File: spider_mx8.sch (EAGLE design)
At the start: 4 parts, among them IC1 AVR-MEGA8-PPTH, J1 AVR_SPI_PRG_6NS

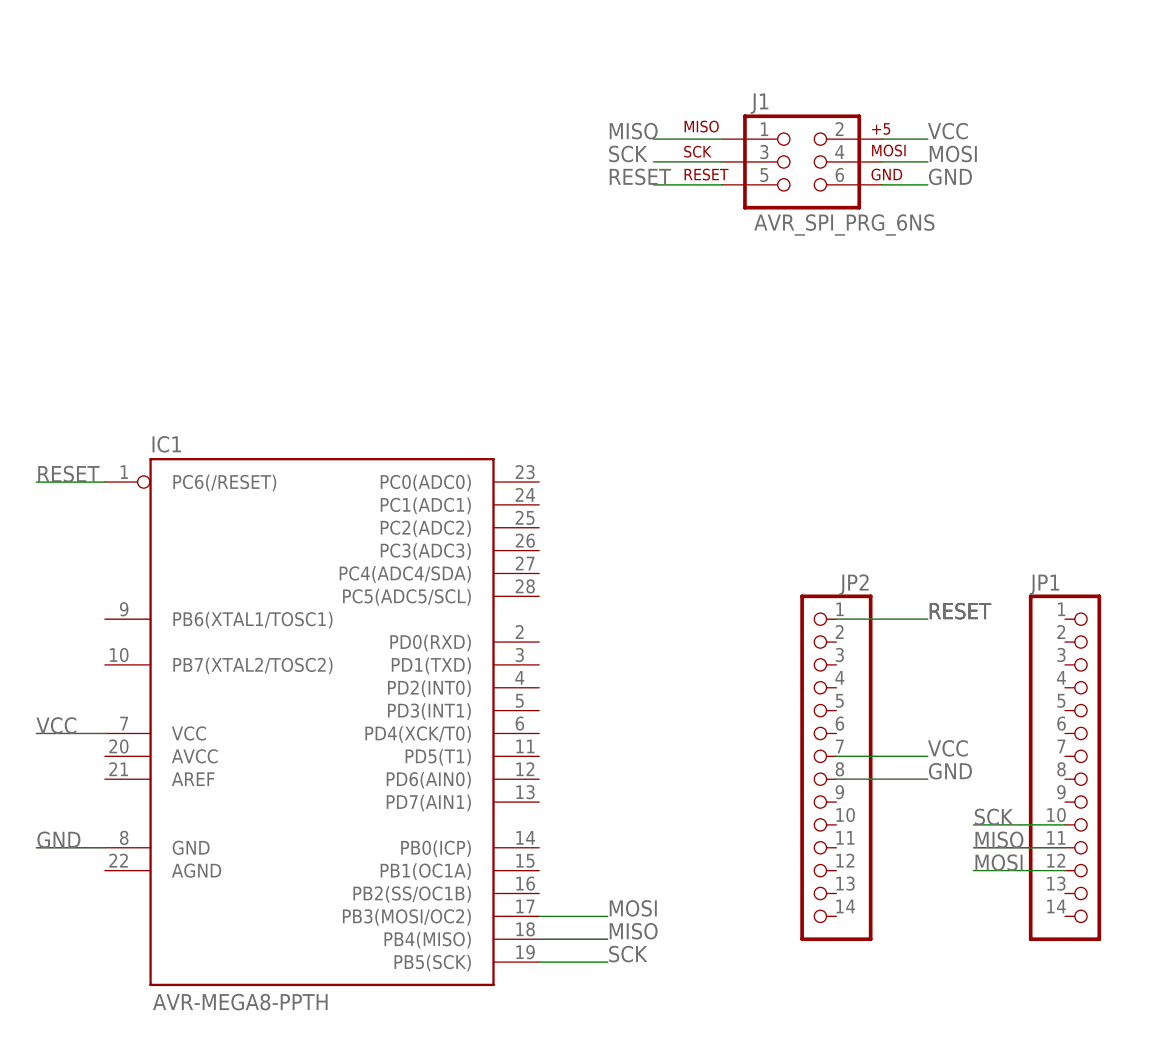
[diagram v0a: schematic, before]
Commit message: added led and cap.  noticed all on bottom side
so I'll need to re-do all this with at least SMT parts on the top
if I want to keep it quasi-one-layer, I'll need to flip wires to top
too.  boo.
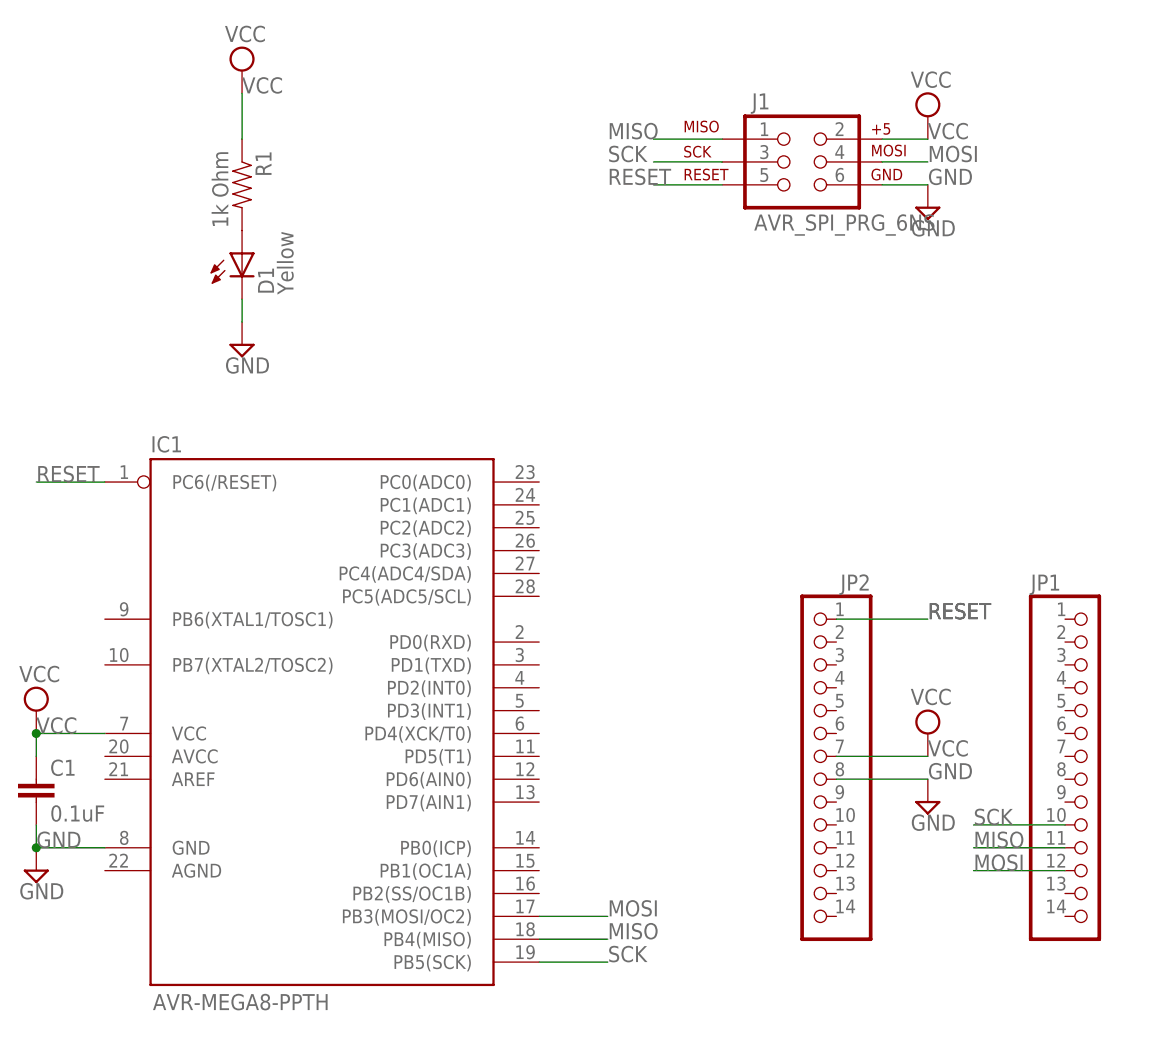
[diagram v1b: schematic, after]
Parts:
- added C1: 0.1uF, SparkFun-Passives:CAP1206
- added D1: Yellow, SparkFun-LED:LED-YELLOWLILYPAD
- added R1: 1k Ohm, SparkFun-Passives:RESISTOR1206
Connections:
- new net N$14: D1.A, R1.2
- net GND: now also C1.2, D1.C
- net VCC: now also C1.1, R1.1
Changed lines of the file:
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@@
 <part name="JP1" library="pinhead" deviceset="PINHD-1X14" device=""/>
 <part name="JP2" library="pinhead" deviceset="PINHD-1X14" device=""/>
+<part name="R1" library="SparkFun-Passives" deviceset="RESISTOR" device="1206" value="1k Ohm"/>
+<part name="D1" library="SparkFun-LED" deviceset="LED-YELLOW" device="LILYPAD" value="Yellow"/>
+<part name="SUPPLY5" library="supply2" deviceset="GND" device=""/>
+<part name="C1" library="SparkFun-Passives" deviceset="CAP" device="1206" value="0.1uF"/>
+<part name="SUPPLY1" library="supply2" deviceset="VCC" device=""/>
+<part name="SUPPLY2" library="supply2" deviceset="VCC" device=""/>
+<part name="SUPPLY3" library="supply2" deviceset="VCC" device=""/>
+<part name="SUPPLY6" library="supply2" deviceset="VCC" device=""/>
+<part name="SUPPLY8" library="supply2" deviceset="GND" device=""/>
+<part name="SUPPLY9" library="supply2" deviceset="GND" device=""/>
+<part name="SUPPLY10" library="supply2" deviceset="GND" device=""/>
 </parts>
 <sheets>
@@
 <instance part="JP1" gate="A" x="86.36" y="-2.54"/>
 <instance part="JP2" gate="A" x="55.88" y="-2.54" rot="MR0"/>
+<instance part="R1" gate="G$1" x="-7.62" y="60.96" rot="R270"/>
+<instance part="D1" gate="G$1" x="-7.62" y="53.34"/>
+<instance part="SUPPLY5" gate="GND" x="-7.62" y="43.18"/>
+<instance part="C1" gate="G$1" x="-30.48" y="-7.62"/>
+<instance part="SUPPLY1" gate="G$1" x="-7.62" y="73.66"/>
+<instance part="SUPPLY2" gate="G$1" x="68.58" y="68.58"/>
+<instance part="SUPPLY3" gate="G$1" x="-30.48" y="2.54"/>
+<instance part="SUPPLY6" gate="G$1" x="68.58" y="0"/>
+<instance part="SUPPLY8" gate="GND" x="68.58" y="58.42"/>
+<instance part="SUPPLY9" gate="GND" x="68.58" y="-7.62"/>
+<instance part="SUPPLY10" gate="GND" x="-30.48" y="-15.24"/>
 </instances>
 <busses>
@@
 <wire x1="-22.86" y1="0" x2="-30.48" y2="0" width="0.1524" layer="91"/>
 <label x="-30.48" y="0" size="1.778" layer="95"/>
+<pinref part="SUPPLY3" gate="G$1" pin="VCC"/>
+<pinref part="C1" gate="G$1" pin="1"/>
+<wire x1="-30.48" y1="0" x2="-30.48" y2="-2.54" width="0.1524" layer="91"/>
+<junction x="-30.48" y="0"/>
 </segment>
 <segment>
@@
 <wire x1="63.5" y1="66.04" x2="68.58" y2="66.04" width="0.1524" layer="91"/>
 <label x="68.58" y="66.04" size="1.778" layer="95"/>
+<pinref part="SUPPLY2" gate="G$1" pin="VCC"/>
 </segment>
 <segment>
@@
 <wire x1="58.42" y1="-2.54" x2="68.58" y2="-2.54" width="0.1524" layer="91"/>
 <label x="68.58" y="-2.54" size="1.778" layer="95"/>
+<pinref part="SUPPLY6" gate="G$1" pin="VCC"/>
+</segment>
+<segment>
+<pinref part="R1" gate="G$1" pin="1"/>
+<wire x1="-7.62" y1="66.04" x2="-7.62" y2="71.12" width="0.1524" layer="91"/>
+<label x="-7.62" y="71.12" size="1.778" layer="95"/>
+<pinref part="SUPPLY1" gate="G$1" pin="VCC"/>
 </segment>
 </net>
@@
 <wire x1="-22.86" y1="-12.7" x2="-30.48" y2="-12.7" width="0.1524" layer="91"/>
 <label x="-30.48" y="-12.7" size="1.778" layer="95"/>
+<pinref part="SUPPLY10" gate="GND" pin="GND"/>
+<pinref part="C1" gate="G$1" pin="2"/>
+<wire x1="-30.48" y1="-10.16" x2="-30.48" y2="-12.7" width="0.1524" layer="91"/>
+<junction x="-30.48" y="-12.7"/>
 </segment>
 <segment>
@@
 <wire x1="63.5" y1="60.96" x2="68.58" y2="60.96" width="0.1524" layer="91"/>
 <label x="68.58" y="60.96" size="1.778" layer="95"/>
+<pinref part="SUPPLY8" gate="GND" pin="GND"/>
 </segment>
 <segment>
@@
 <wire x1="58.42" y1="-5.08" x2="68.58" y2="-5.08" width="0.1524" layer="91"/>
 <label x="68.58" y="-5.08" size="1.778" layer="95"/>
+<pinref part="SUPPLY9" gate="GND" pin="GND"/>
+</segment>
+<segment>
+<pinref part="D1" gate="G$1" pin="C"/>
+<pinref part="SUPPLY5" gate="GND" pin="GND"/>
+<wire x1="-7.62" y1="48.26" x2="-7.62" y2="45.72" width="0.1524" layer="91"/>
 </segment>
 </net>
+<net name="N$14" class="0">
+<segment>
+<pinref part="R1" gate="G$1" pin="2"/>
+<pinref part="D1" gate="G$1" pin="A"/>
+</segment>
+</net>

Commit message: printed this version out.  works.  sexy.
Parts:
- removed IC1: AVR-MEGA8-PPTH, SparkFun-DigitalIC:AVR-MEGA8-PPTH
- removed JP1, JP2: (no value), pinhead:PINHD-1X14
- added JP3, JP4: M14, SparkFun-Connectors:M14
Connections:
- net GND: now also JP3.8; no longer IC1.GND@1, JP2.8
- net MISO: now also JP4.11; no longer IC1.PB4(MISO), JP1.11
- net MOSI: now also JP4.12; no longer IC1.PB3(MOSI/OC2), JP1.12
- net RESET: now also JP3.1; no longer IC1.PC6(/RESET), JP2.1
- net SCK: now also JP4.10; no longer IC1.PB5(SCK), JP1.10
- net VCC: now also JP3.7; no longer IC1.VCC@1, JP2.7
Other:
- moved on the sheet: C1
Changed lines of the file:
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@@
 </classes>
 <parts>
-<part name="IC1" library="SparkFun-DigitalIC" deviceset="AVR-MEGA8-P" device="PTH"/>
 <part name="J1" library="SparkFun-Connectors" deviceset="AVR_SPI_PRG_6" device="NS"/>
-<part name="JP1" library="pinhead" deviceset="PINHD-1X14" device=""/>
-<part name="JP2" library="pinhead" deviceset="PINHD-1X14" device=""/>
 <part name="R1" library="SparkFun-Passives" deviceset="RESISTOR" device="1206" value="1k Ohm"/>
 <part name="D1" library="SparkFun-LED" deviceset="LED-YELLOW" device="LILYPAD" value="Yellow"/>
@@
 <part name="SUPPLY9" library="supply2" deviceset="GND" device=""/>
 <part name="SUPPLY10" library="supply2" deviceset="GND" device=""/>
+<part name="JP3" library="SparkFun-Connectors" deviceset="M14" device=""/>
+<part name="JP4" library="SparkFun-Connectors" deviceset="M14" device=""/>
 </parts>
 <sheets>
@@
 </plain>
 <instances>
-<instance part="IC1" gate="G$1" x="0" y="0"/>
 <instance part="J1" gate="G$1" x="53.34" y="63.5"/>
-<instance part="JP1" gate="A" x="86.36" y="-2.54"/>
-<instance part="JP2" gate="A" x="55.88" y="-2.54" rot="MR0"/>
 <instance part="R1" gate="G$1" x="-7.62" y="60.96" rot="R270"/>
 <instance part="D1" gate="G$1" x="-7.62" y="53.34"/>
 <instance part="SUPPLY5" gate="GND" x="-7.62" y="43.18"/>
-<instance part="C1" gate="G$1" x="-30.48" y="-7.62"/>
+<instance part="C1" gate="G$1" x="-20.32" y="-5.08"/>
 <instance part="SUPPLY1" gate="G$1" x="-7.62" y="73.66"/>
 <instance part="SUPPLY2" gate="G$1" x="68.58" y="68.58"/>
-<instance part="SUPPLY3" gate="G$1" x="-30.48" y="2.54"/>
+<instance part="SUPPLY3" gate="G$1" x="-20.32" y="5.08"/>
 <instance part="SUPPLY6" gate="G$1" x="68.58" y="0"/>
 <instance part="SUPPLY8" gate="GND" x="68.58" y="58.42"/>
 <instance part="SUPPLY9" gate="GND" x="68.58" y="-7.62"/>
-<instance part="SUPPLY10" gate="GND" x="-30.48" y="-15.24"/>
+<instance part="SUPPLY10" gate="GND" x="-20.32" y="-12.7"/>
+<instance part="JP3" gate="G$1" x="50.8" y="-5.08" rot="MR180"/>
+<instance part="JP4" gate="G$1" x="91.44" y="-5.08" rot="R180"/>
 </instances>
 <busses>
@@
 <net name="SCK" class="0">
 <segment>
-<pinref part="IC1" gate="G$1" pin="PB5(SCK)"/>
-<wire x1="25.4" y1="-25.4" x2="33.02" y2="-25.4" width="0.1524" layer="91"/>
-<label x="33.02" y="-25.4" size="1.778" layer="95"/>
-</segment>
-<segment>
 <pinref part="J1" gate="G$1" pin="3"/>
 <wire x1="45.72" y1="63.5" x2="38.1" y2="63.5" width="0.1524" layer="91"/>
@@
 </segment>
 <segment>
-<pinref part="JP1" gate="A" pin="10"/>
-<wire x1="83.82" y1="-10.16" x2="73.66" y2="-10.16" width="0.1524" layer="91"/>
+<wire x1="83.82" y1="-10.16" x2="81.28" y2="-10.16" width="0.1524" layer="91"/>
 <label x="73.66" y="-10.16" size="1.778" layer="95"/>
+<pinref part="JP4" gate="G$1" pin="10"/>
+<wire x1="81.28" y1="-10.16" x2="73.66" y2="-10.16" width="0.1524" layer="91"/>
+<junction x="81.28" y="-10.16"/>
 </segment>
 </net>
 <net name="MISO" class="0">
-<segment>
-<pinref part="IC1" gate="G$1" pin="PB4(MISO)"/>
-<wire x1="25.4" y1="-22.86" x2="33.02" y2="-22.86" width="0.1524" layer="91"/>
-<label x="33.02" y="-22.86" size="1.778" layer="95"/>
-</segment>
 <segment>
 <pinref part="J1" gate="G$1" pin="1"/>
@@
 </segment>
 <segment>
-<pinref part="JP1" gate="A" pin="11"/>
-<wire x1="83.82" y1="-12.7" x2="73.66" y2="-12.7" width="0.1524" layer="91"/>
+<wire x1="83.82" y1="-12.7" x2="81.28" y2="-12.7" width="0.1524" layer="91"/>
 <label x="73.66" y="-12.7" size="1.778" layer="95"/>
+<pinref part="JP4" gate="G$1" pin="11"/>
+<wire x1="81.28" y1="-12.7" x2="73.66" y2="-12.7" width="0.1524" layer="91"/>
+<junction x="81.28" y="-12.7"/>
 </segment>
 </net>
 <net name="MOSI" class="0">
-<segment>
-<pinref part="IC1" gate="G$1" pin="PB3(MOSI/OC2)"/>
-<wire x1="25.4" y1="-20.32" x2="33.02" y2="-20.32" width="0.1524" layer="91"/>
-<label x="33.02" y="-20.32" size="1.778" layer="95"/>
-</segment>
 <segment>
 <pinref part="J1" gate="G$1" pin="4"/>
@@
 </segment>
 <segment>
-<pinref part="JP1" gate="A" pin="12"/>
-<wire x1="83.82" y1="-15.24" x2="73.66" y2="-15.24" width="0.1524" layer="91"/>
+<wire x1="83.82" y1="-15.24" x2="81.28" y2="-15.24" width="0.1524" layer="91"/>
 <label x="73.66" y="-15.24" size="1.778" layer="95"/>
+<pinref part="JP4" gate="G$1" pin="12"/>
+<wire x1="81.28" y1="-15.24" x2="73.66" y2="-15.24" width="0.1524" layer="91"/>
+<junction x="81.28" y="-15.24"/>
 </segment>
 </net>
 <net name="RESET" class="0">
-<segment>
-<pinref part="IC1" gate="G$1" pin="PC6(/RESET)"/>
-<wire x1="-22.86" y1="27.94" x2="-30.48" y2="27.94" width="0.1524" layer="91"/>
-<label x="-30.48" y="27.94" size="1.778" layer="95"/>
-</segment>
 <segment>
 <pinref part="J1" gate="G$1" pin="5"/>
@@
 </segment>
 <segment>
-<pinref part="JP2" gate="A" pin="1"/>
-<wire x1="58.42" y1="12.7" x2="68.58" y2="12.7" width="0.1524" layer="91"/>
+<wire x1="60.96" y1="12.7" x2="68.58" y2="12.7" width="0.1524" layer="91"/>
 <label x="68.58" y="12.7" size="1.778" layer="95"/>
 <label x="68.58" y="12.7" size="1.778" layer="95"/>
+<pinref part="JP3" gate="G$1" pin="1"/>
 </segment>
 </net>
 <net name="VCC" class="0">
 <segment>
-<pinref part="IC1" gate="G$1" pin="VCC@1"/>
-<wire x1="-22.86" y1="0" x2="-30.48" y2="0" width="0.1524" layer="91"/>
-<label x="-30.48" y="0" size="1.778" layer="95"/>
+<label x="-20.32" y="2.54" size="1.778" layer="95"/>
 <pinref part="SUPPLY3" gate="G$1" pin="VCC"/>
 <pinref part="C1" gate="G$1" pin="1"/>
-<wire x1="-30.48" y1="0" x2="-30.48" y2="-2.54" width="0.1524" layer="91"/>
-<junction x="-30.48" y="0"/>
+<wire x1="-20.32" y1="2.54" x2="-20.32" y2="0" width="0.1524" layer="91"/>
 </segment>
 <segment>
@@
 </segment>
 <segment>
-<pinref part="JP2" gate="A" pin="7"/>
-<wire x1="58.42" y1="-2.54" x2="68.58" y2="-2.54" width="0.1524" layer="91"/>
+<wire x1="60.96" y1="-2.54" x2="68.58" y2="-2.54" width="0.1524" layer="91"/>
 <label x="68.58" y="-2.54" size="1.778" layer="95"/>
 <pinref part="SUPPLY6" gate="G$1" pin="VCC"/>
+<pinref part="JP3" gate="G$1" pin="7"/>
 </segment>
 <segment>
@@
 <net name="GND" class="0">
 <segment>
-<pinref part="IC1" gate="G$1" pin="GND@1"/>
-<wire x1="-22.86" y1="-12.7" x2="-30.48" y2="-12.7" width="0.1524" layer="91"/>
-<label x="-30.48" y="-12.7" size="1.778" layer="95"/>
+<label x="-20.32" y="-10.16" size="1.778" layer="95"/>
 <pinref part="SUPPLY10" gate="GND" pin="GND"/>
 <pinref part="C1" gate="G$1" pin="2"/>
-<wire x1="-30.48" y1="-10.16" x2="-30.48" y2="-12.7" width="0.1524" layer="91"/>
-<junction x="-30.48" y="-12.7"/>
+<wire x1="-20.32" y1="-7.62" x2="-20.32" y2="-10.16" width="0.1524" layer="91"/>
 </segment>
 <segment>
@@
 </segment>
 <segment>
-<pinref part="JP2" gate="A" pin="8"/>
-<wire x1="58.42" y1="-5.08" x2="68.58" y2="-5.08" width="0.1524" layer="91"/>
+<wire x1="60.96" y1="-5.08" x2="68.58" y2="-5.08" width="0.1524" layer="91"/>
 <label x="68.58" y="-5.08" size="1.778" layer="95"/>
 <pinref part="SUPPLY9" gate="GND" pin="GND"/>
+<pinref part="JP3" gate="G$1" pin="8"/>
 </segment>
 <segment>
